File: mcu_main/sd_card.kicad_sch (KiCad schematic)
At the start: 4 parts, among them J1 Micro_SD_Card_Det_Hirose_DM3AT

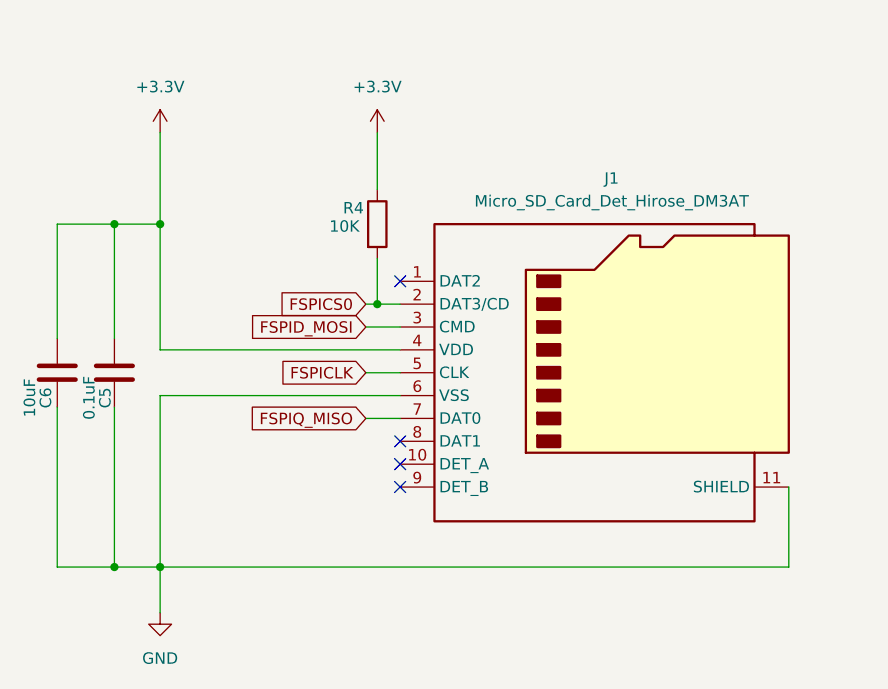
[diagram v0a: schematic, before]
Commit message: added I2C lines
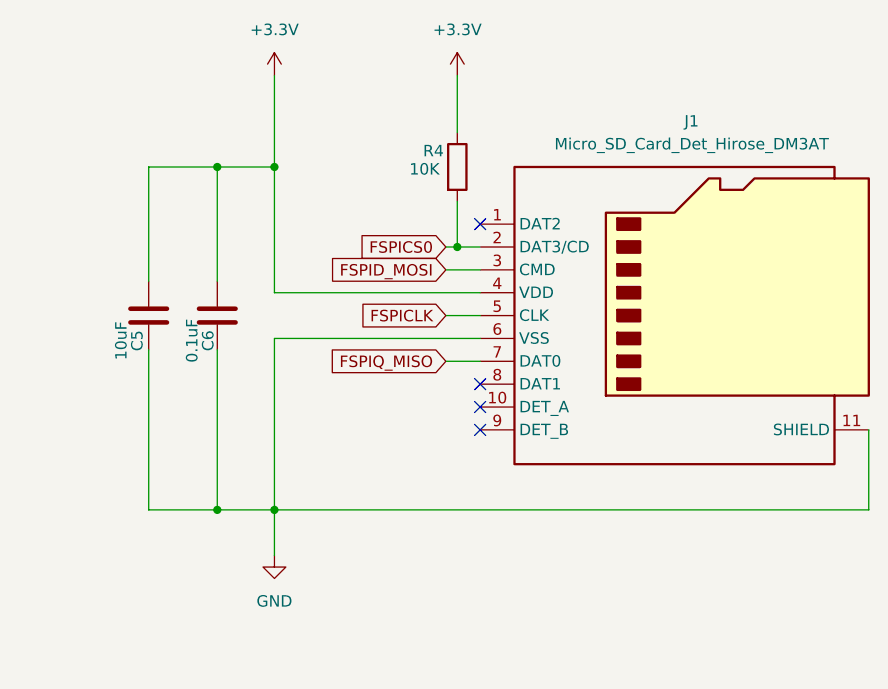
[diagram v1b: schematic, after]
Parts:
- renumbered C6 to C5, C5 to C6
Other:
- moved on the sheet: C5, C6, J1, R4

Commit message: SD card sheet now fits
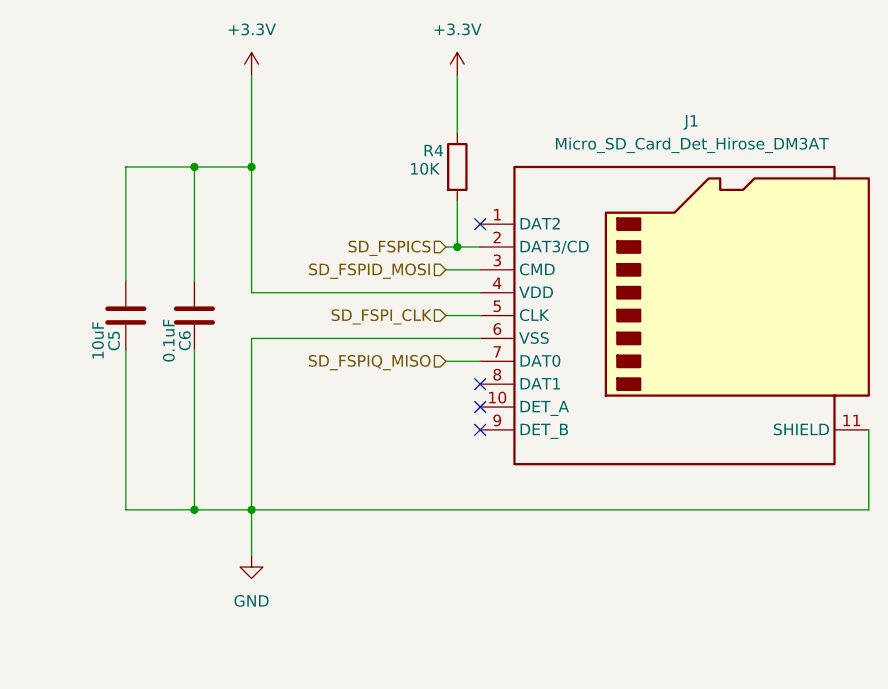
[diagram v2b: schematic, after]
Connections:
- net FSPICLK renamed SD_FSPI_CLK
- net FSPICS0 renamed SD_FSPICS
- net FSPID_MOSI renamed SD_FSPID_MOSI
- net FSPIQ_MISO renamed SD_FSPIQ_MISO
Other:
- moved on the sheet: C5, C6
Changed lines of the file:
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@@
 	(paper "A4")
 	(junction
-		(at 119.38 80.01)
+		(at 116.84 80.01)
 		(diameter 0)
 		(color 0 0 0 0)
@@
 	)
 	(junction
-		(at 119.38 118.11)
+		(at 116.84 118.11)
 		(diameter 0)
 		(color 0 0 0 0)
 	)
 	(junction
-		(at 113.03 118.11)
+		(at 110.49 118.11)
 		(diameter 0)
 		(color 0 0 0 0)
 	)
 	(junction
-		(at 113.03 80.01)
+		(at 110.49 80.01)
 		(diameter 0)
 		(color 0 0 0 0)
@@
 	(wire
 		(pts
-			(xy 105.41 92.71) (xy 105.41 80.01)
-		)
-		(stroke
-			(width 0)
-			(type default)
-		)
-	)
-	(wire
-		(pts
-			(xy 119.38 99.06) (xy 119.38 118.11)
-		)
-		(stroke
-			(width 0)
-			(type default)
-		)
-	)
-	(wire
-		(pts
-			(xy 113.03 100.33) (xy 113.03 118.11)
+			(xy 102.87 92.71) (xy 102.87 80.01)
+		)
+		(stroke
+			(width 0)
+			(type default)
+		)
+	)
+	(wire
+		(pts
+			(xy 116.84 99.06) (xy 116.84 118.11)
+		)
+		(stroke
+			(width 0)
+			(type default)
+		)
+	)
+	(wire
+		(pts
+			(xy 110.49 100.33) (xy 110.49 118.11)
 		)
 		(stroke
@@
 	(wire
 		(pts
-			(xy 119.38 93.98) (xy 142.24 93.98)
-		)
-		(stroke
-			(width 0)
-			(type default)
-		)
-	)
-	(wire
-		(pts
-			(xy 119.38 80.01) (xy 119.38 93.98)
+			(xy 116.84 93.98) (xy 142.24 93.98)
+		)
+		(stroke
+			(width 0)
+			(type default)
+		)
+	)
+	(wire
+		(pts
+			(xy 116.84 80.01) (xy 116.84 93.98)
 		)
 		(stroke
@@
 	(wire
 		(pts
-			(xy 119.38 69.85) (xy 119.38 80.01)
+			(xy 116.84 69.85) (xy 116.84 80.01)
 		)
 		(stroke
@@
 	(wire
 		(pts
-			(xy 119.38 99.06) (xy 142.24 99.06)
+			(xy 116.84 99.06) (xy 142.24 99.06)
 		)
 		(stroke
@@
 	(wire
 		(pts
-			(xy 105.41 100.33) (xy 105.41 118.11)
-		)
-		(stroke
-			(width 0)
-			(type default)
-		)
-	)
-	(wire
-		(pts
-			(xy 119.38 123.19) (xy 119.38 118.11)
+			(xy 102.87 100.33) (xy 102.87 118.11)
+		)
+		(stroke
+			(width 0)
+			(type default)
+		)
+	)
+	(wire
+		(pts
+			(xy 116.84 123.19) (xy 116.84 118.11)
 		)
 		(stroke
@@
 	(wire
 		(pts
-			(xy 113.03 80.01) (xy 119.38 80.01)
-		)
-		(stroke
-			(width 0)
-			(type default)
-		)
-	)
-	(wire
-		(pts
-			(xy 113.03 118.11) (xy 119.38 118.11)
-		)
-		(stroke
-			(width 0)
-			(type default)
-		)
-	)
-	(wire
-		(pts
-			(xy 119.38 118.11) (xy 185.42 118.11)
+			(xy 110.49 80.01) (xy 116.84 80.01)
+		)
+		(stroke
+			(width 0)
+			(type default)
+		)
+	)
+	(wire
+		(pts
+			(xy 110.49 118.11) (xy 116.84 118.11)
+		)
+		(stroke
+			(width 0)
+			(type default)
+		)
+	)
+	(wire
+		(pts
+			(xy 116.84 118.11) (xy 185.42 118.11)
 		)
 		(stroke
@@
 	(wire
 		(pts
-			(xy 113.03 92.71) (xy 113.03 80.01)
+			(xy 110.49 92.71) (xy 110.49 80.01)
 		)
 		(stroke
@@
 	(wire
 		(pts
-			(xy 105.41 118.11) (xy 113.03 118.11)
-		)
-		(stroke
-			(width 0)
-			(type default)
-		)
-	)
-	(wire
-		(pts
-			(xy 105.41 80.01) (xy 113.03 80.01)
-		)
-		(stroke
-			(width 0)
-			(type default)
-		)
-	)
-	(global_label "FSPICLK"
+			(xy 102.87 118.11) (xy 110.49 118.11)
+		)
+		(stroke
+			(width 0)
+			(type default)
+		)
+	)
+	(wire
+		(pts
+			(xy 102.87 80.01) (xy 110.49 80.01)
+		)
+		(stroke
+			(width 0)
+			(type default)
+		)
+	)
+	(hierarchical_label "SD_FSPI_CLK"
 		(shape input)
 		(at 138.43 96.52 180)
-		(fields_autoplaced yes)
 		(effects
 			(font
@@
 			(justify right)
 		)
-		(property "Intersheetrefs" "${INTERSHEET_REFS}"
-			(at 127.7038 96.52 0)
-			(effects
-				(font
-					(size 1.27 1.27)
-				)
-				(justify right)
-				(hide yes)
-			)
-		)
-	)
-	(global_label "FSPID_MOSI"
+	)
+	(hierarchical_label "SD_FSPIQ_MISO"
 		(shape input)
-		(at 138.43 91.44 180)
-		(fields_autoplaced yes)
+		(at 138.43 101.6 180)
 		(effects
 			(font
@@
 			(justify right)
 		)
-		(property "Intersheetrefs" "${INTERSHEET_REFS}"
-			(at 124.4381 91.44 0)
-			(effects
-				(font
-					(size 1.27 1.27)
-				)
-				(justify right)
-				(hide yes)
-			)
-		)
-	)
-	(global_label "FSPICS0"
+	)
+	(hierarchical_label "SD_FSPID_MOSI"
 		(shape input)
-		(at 138.43 88.9 180)
-		(fields_autoplaced yes)
+		(at 138.43 91.44 180)
 		(effects
 			(font
@@
 			(justify right)
 		)
-		(property "Intersheetrefs" "${INTERSHEET_REFS}"
-			(at 127.5829 88.9 0)
-			(effects
-				(font
-					(size 1.27 1.27)
-				)
-				(justify right)
-				(hide yes)
-			)
-		)
-	)
-	(global_label "FSPIQ_MISO"
+	)
+	(hierarchical_label "SD_FSPICS"
 		(shape input)
-		(at 138.43 101.6 180)
-		(fields_autoplaced yes)
+		(at 138.43 88.9 180)
 		(effects
 			(font
@@
 			(justify right)
 		)
-		(property "Intersheetrefs" "${INTERSHEET_REFS}"
-			(at 124.3776 101.6 0)
-			(effects
-				(font
-					(size 1.27 1.27)
-				)
-				(justify right)
-				(hide yes)
-			)
-		)
 	)
 	(symbol
 		(lib_id "power:+3.3V")
-		(at 119.38 69.85 0)
+		(at 116.84 69.85 0)
 		(unit 1)
 		(exclude_from_sim no)
@@
 		(fields_autoplaced yes)
 		(property "Reference" "#PWR?"
-			(at 119.38 73.66 0)
+			(at 116.84 73.66 0)
 			(effects
 				(font
@@
 		)
 		(property "Value" "+3.3V"
-			(at 119.38 64.77 0)
+			(at 116.84 64.77 0)
 			(effects
 				(font
@@
 		)
 		(property "Footprint" ""
-			(at 119.38 69.85 0)
+			(at 116.84 69.85 0)
 			(effects
 				(font
@@
 		)
 		(property "Datasheet" ""
-			(at 119.38 69.85 0)
+			(at 116.84 69.85 0)
 			(effects
 				(font
@@
 		)
 		(property "Description" "Power symbol creates a global label with name \"+3.3V\""
-			(at 119.38 69.85 0)
+			(at 116.84 69.85 0)
 			(effects
 				(font
@@
 	(symbol
 		(lib_id "Device:C")
-		(at 113.03 96.52 0)
+		(at 110.49 96.52 0)
 		(unit 1)
 		(exclude_from_sim no)
@@
 		(dnp no)
 		(property "Reference" "C6"
-			(at 112.014 99.314 90)
+			(at 109.474 99.314 90)
 			(effects
 				(font
@@
 		)
 		(property "Value" "0.1uF"
-			(at 110.236 99.314 90)
+			(at 107.696 99.314 90)
 			(effects
 				(font
@@
 		)
 		(property "Footprint" "Capacitor_SMD:C_0603_1608Metric_Pad1.08x0.95mm_HandSolder"
-			(at 113.9952 100.33 0)
+			(at 111.4552 100.33 0)
 			(effects
 				(font
@@
 		)
 		(property "Datasheet" "~"
-			(at 113.03 96.52 0)
+			(at 110.49 96.52 0)
 			(effects
 				(font
@@
 		)
 		(property "Description" "Unpolarized capacitor"
-			(at 113.03 96.52 0)
+			(at 110.49 96.52 0)
 			(effects
 				(font
@@
 	(symbol
 		(lib_id "Device:C")
-		(at 105.41 96.52 0)
+		(at 102.87 96.52 0)
 		(unit 1)
 		(exclude_from_sim no)
@@
 		(dnp no)
 		(property "Reference" "C5"
-			(at 104.14 99.314 90)
+			(at 101.6 99.314 90)
 			(effects
 				(font
@@
 		)
 		(property "Value" "10uF"
-			(at 102.362 99.314 90)
+			(at 99.822 99.314 90)
 			(effects
 				(font
@@
 		)
 		(property "Footprint" "Capacitor_SMD:C_0603_1608Metric_Pad1.08x0.95mm_HandSolder"
-			(at 106.3752 100.33 0)
+			(at 103.8352 100.33 0)
 			(effects
 				(font
@@
 		)
 		(property "Datasheet" "~"
-			(at 105.41 96.52 0)
+			(at 102.87 96.52 0)
 			(effects
 				(font
@@
 		)
 		(property "Description" "Unpolarized capacitor"
-			(at 105.41 96.52 0)
+			(at 102.87 96.52 0)
 			(effects
 				(font
@@
 	(symbol
 		(lib_id "power:GND")
-		(at 119.38 123.19 0)
+		(at 116.84 123.19 0)
 		(unit 1)
 		(exclude_from_sim no)
@@
 		(fields_autoplaced yes)
 		(property "Reference" "#PWR?"
-			(at 119.38 129.54 0)
+			(at 116.84 129.54 0)
 			(effects
 				(font
@@
 		)
 		(property "Value" "GND"
-			(at 119.38 128.27 0)
+			(at 116.84 128.27 0)
 			(effects
 				(font
@@
 		)
 		(property "Footprint" ""
-			(at 119.38 123.19 0)
+			(at 116.84 123.19 0)
 			(effects
 				(font
@@
 		)
 		(property "Datasheet" ""
-			(at 119.38 123.19 0)
+			(at 116.84 123.19 0)
 			(effects
 				(font
@@
 		)
 		(property "Description" "Power symbol creates a global label with name \"GND\" , ground"
-			(at 119.38 123.19 0)
-			(effects
-				(font
+			(at 116.84 123.19 0)
+			(effects
+				(font
